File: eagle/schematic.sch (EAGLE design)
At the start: 32 parts, among them U1 PIC18F252-I/SP

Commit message: PCB in progress
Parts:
- added 5V, AN0, VBAT: TPPAD1-13, testpad:TPPAD1-13
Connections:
- net 5V: now also 5V.TP
- net AN0: now also AN0.TP
- net VBAT: now also VBAT.TP
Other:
- note added: "Title: PIC18F252 Binary Clock Author: Michel Lavoie Revision: 0.1.0 Date: 2016-11-26"
- note removed: "0.1.0"
- note removed: "1/1"
- note removed: "PIC18F252 Binary Clock"
- moved on the sheet: ADJ, BAT, C1, D1, D2, HR, MIN, PROG, R1, R10, R11, R12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

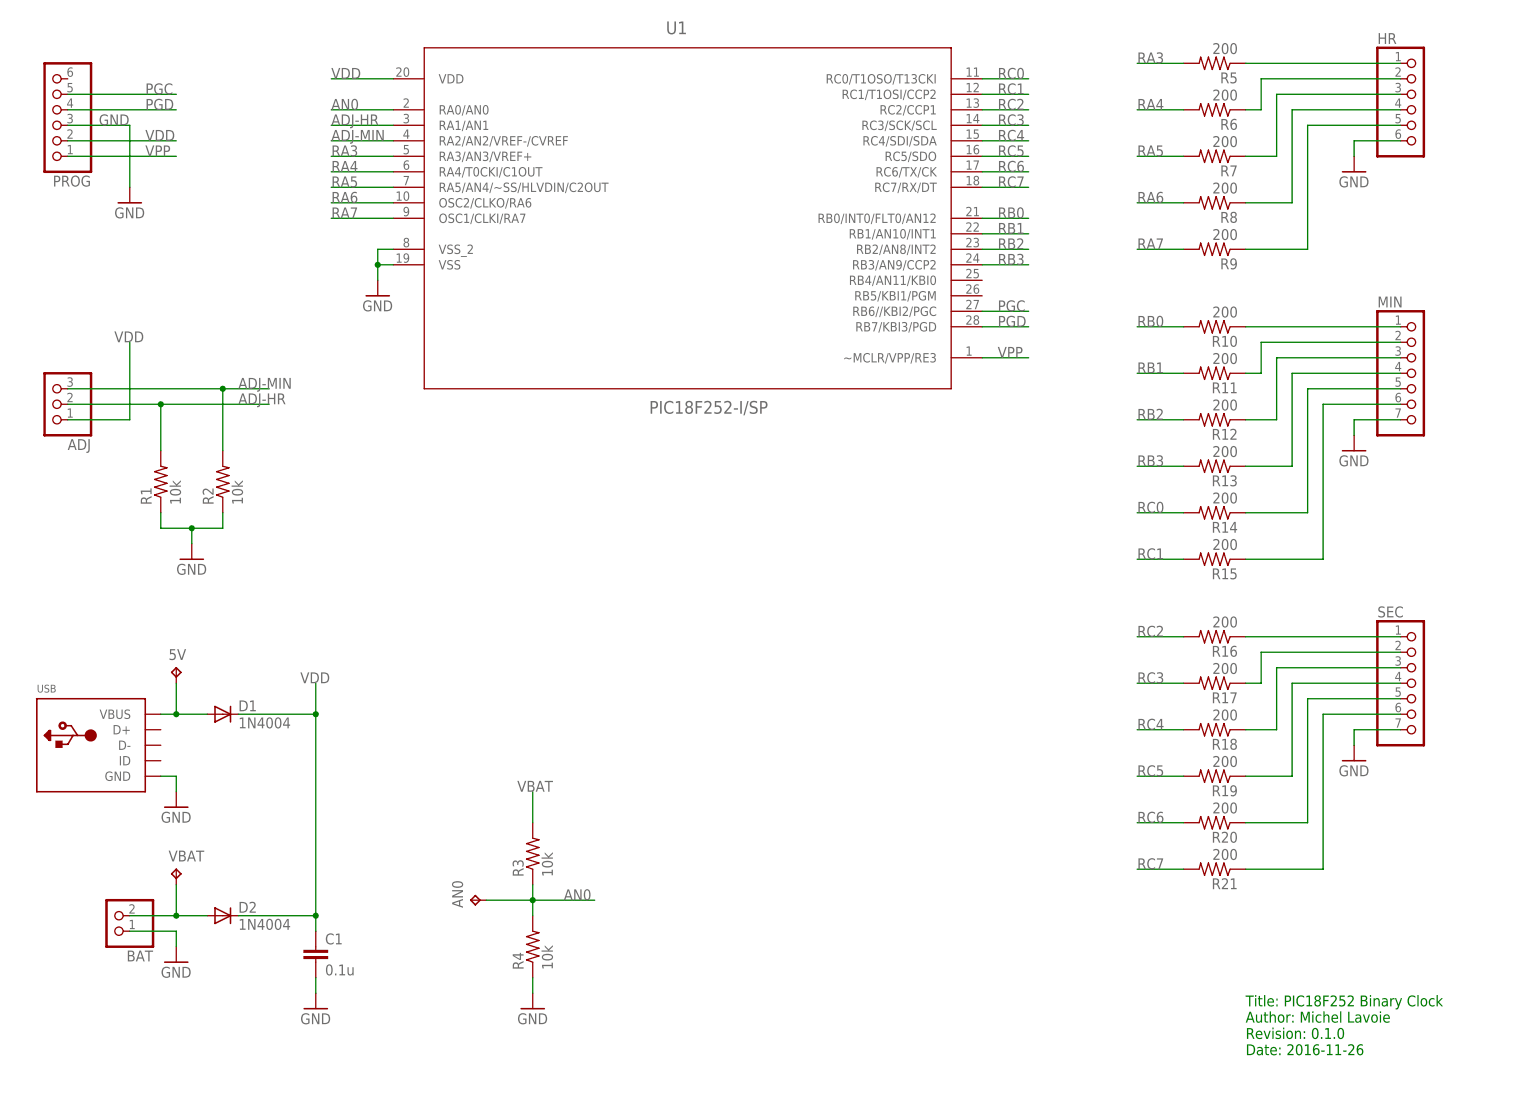
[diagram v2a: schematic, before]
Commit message: Version 0.1.1. Applied all items in the To Do list.
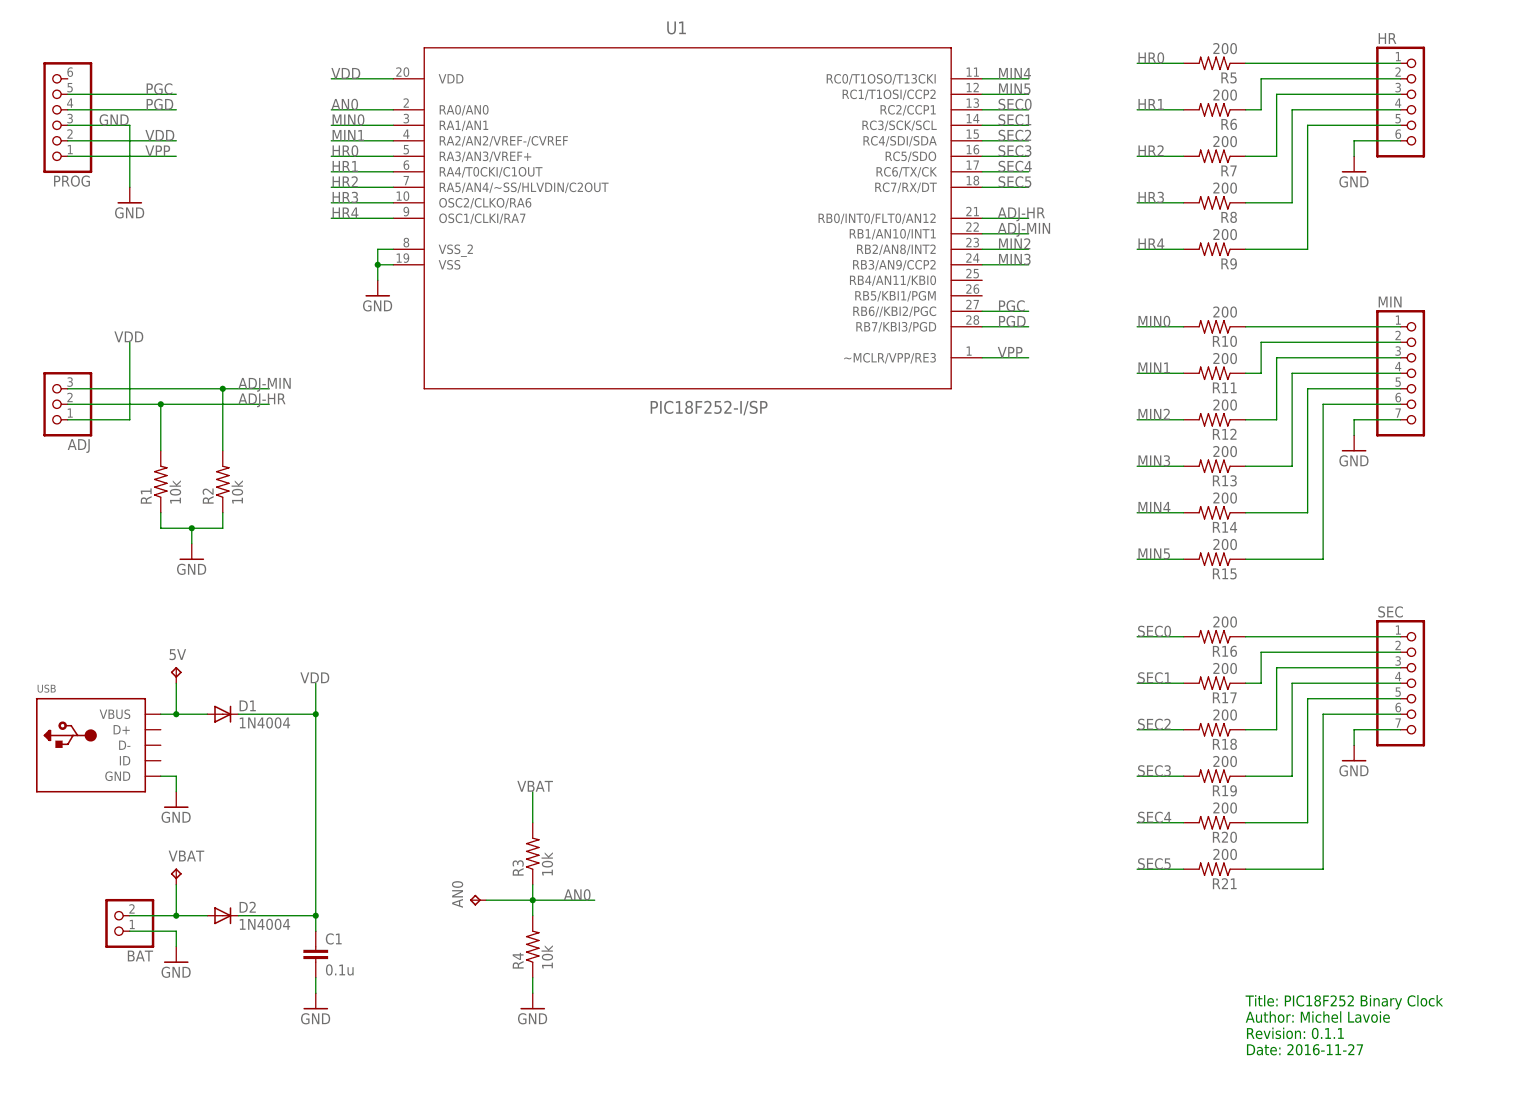
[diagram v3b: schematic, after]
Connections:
- net RA3 renamed HR0
- net RA4 renamed HR1
- net RA5 renamed HR2
- net RA6 renamed HR3
- net RA7 renamed HR4
- net RB2 renamed MIN2
- net RB3 renamed MIN3
- net RC0 renamed MIN4
- net RC1 renamed MIN5
- net RC2 renamed SEC0
- net RC3 renamed SEC1
- net RC4 renamed SEC2
- net RC5 renamed SEC3
- net RC6 renamed SEC4
- net RC7 renamed SEC5
- removed net RB0: R10.2, U1.RB0/INT0/FLT0/AN12
- removed net RB1: R11.2, U1.RB1/AN10/INT1
- new net MIN0: R10.2, U1.RA1/AN1
- new net MIN1: R11.2, U1.RA2/AN2/VREF-/CVREF
- net ADJ-HR: now also U1.RB0/INT0/FLT0/AN12; no longer U1.RA1/AN1
- net ADJ-MIN: now also U1.RB1/AN10/INT1; no longer U1.RA2/AN2/VREF-/CVREF
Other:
- note added: "Title: PIC18F252 Binary Clock Author: Michel Lavoie Revision: 0.1.1 Date: 2016-11-27"
- note removed: "Title: PIC18F252 Binary Clock Author: Michel Lavoie Revision: 0.1.0 Date: 2016-11-26"
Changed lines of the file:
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@@
 <text x="208.28" y="7.62" size="1.778" layer="91">Title: PIC18F252 Binary Clock
 Author: Michel Lavoie
-Revision: 0.1.0
-Date: 2016-11-26</text>
+Revision: 0.1.1
+Date: 2016-11-27</text>
 </plain>
 <instances>
@@
 </segment>
 <segment>
-<pinref part="U1" gate="A" pin="RA1/AN1"/>
-<wire x1="58.42" y1="160.02" x2="68.58" y2="160.02" width="0.1524" layer="91"/>
-<label x="58.42" y="160.02" size="1.778" layer="95"/>
+<pinref part="U1" gate="A" pin="RB0/INT0/FLT0/AN12"/>
+<wire x1="172.72" y1="144.78" x2="165.1" y2="144.78" width="0.1524" layer="91"/>
+<label x="167.64" y="144.78" size="1.778" layer="95"/>
 </segment>
 </net>
@@
 </segment>
 <segment>
-<pinref part="U1" gate="A" pin="RA2/AN2/VREF-/CVREF"/>
-<wire x1="58.42" y1="157.48" x2="68.58" y2="157.48" width="0.1524" layer="91"/>
-<label x="58.42" y="157.48" size="1.778" layer="95"/>
+<pinref part="U1" gate="A" pin="RB1/AN10/INT1"/>
+<wire x1="172.72" y1="142.24" x2="165.1" y2="142.24" width="0.1524" layer="91"/>
+<label x="167.64" y="142.24" size="1.778" layer="95"/>
 </segment>
 </net>
@@
 </segment>
 </net>
-<net name="RA3" class="0">
+<net name="HR0" class="0">
 <segment>
 <pinref part="U1" gate="A" pin="RA3/AN3/VREF+"/>
@@
 </segment>
 </net>
-<net name="RA4" class="0">
+<net name="HR1" class="0">
 <segment>
 <pinref part="U1" gate="A" pin="RA4/T0CKI/C1OUT"/>
@@
 </segment>
 </net>
-<net name="RA5" class="0">
+<net name="HR2" class="0">
 <segment>
 <pinref part="U1" gate="A" pin="RA5/AN4/~SS/HLVDIN/C2OUT"/>
@@
 </segment>
 </net>
-<net name="RA6" class="0">
+<net name="HR3" class="0">
 <segment>
 <pinref part="U1" gate="A" pin="OSC2/CLKO/RA6"/>
@@
 </segment>
 </net>
-<net name="RA7" class="0">
+<net name="HR4" class="0">
 <segment>
 <pinref part="U1" gate="A" pin="OSC1/CLKI/RA7"/>
@@
 </segment>
 </net>
-<net name="RC0" class="0">
+<net name="MIN4" class="0">
 <segment>
 <pinref part="U1" gate="A" pin="RC0/T1OSO/T13CKI"/>
@@
 </segment>
 </net>
-<net name="RC1" class="0">
+<net name="MIN5" class="0">
 <segment>
 <pinref part="U1" gate="A" pin="RC1/T1OSI/CCP2"/>
@@
 </segment>
 </net>
-<net name="RC2" class="0">
+<net name="SEC0" class="0">
 <segment>
 <pinref part="U1" gate="A" pin="RC2/CCP1"/>
@@
 </segment>
 </net>
-<net name="RC3" class="0">
+<net name="SEC1" class="0">
 <segment>
 <pinref part="U1" gate="A" pin="RC3/SCK/SCL"/>
@@
 </segment>
 </net>
-<net name="RC4" class="0">
+<net name="SEC2" class="0">
 <segment>
 <pinref part="U1" gate="A" pin="RC4/SDI/SDA"/>
@@
 </segment>
 </net>
-<net name="RC5" class="0">
+<net name="SEC3" class="0">
 <segment>
 <pinref part="U1" gate="A" pin="RC5/SDO"/>
@@
 </segment>
 </net>
-<net name="RC6" class="0">
+<net name="SEC4" class="0">
 <segment>
 <pinref part="U1" gate="A" pin="RC6/TX/CK"/>
@@
 </segment>
 </net>
-<net name="RC7" class="0">
+<net name="SEC5" class="0">
 <segment>
 <pinref part="U1" gate="A" pin="RC7/RX/DT"/>
@@
 </segment>
 </net>
-<net name="RB0" class="0">
-<segment>
-<pinref part="U1" gate="A" pin="RB0/INT0/FLT0/AN12"/>
-<wire x1="172.72" y1="144.78" x2="165.1" y2="144.78" width="0.1524" layer="91"/>
-<label x="167.64" y="144.78" size="1.778" layer="95"/>
+<net name="MIN2" class="0">
+<segment>
+<pinref part="U1" gate="A" pin="RB2/AN8/INT2"/>
+<wire x1="172.72" y1="139.7" x2="165.1" y2="139.7" width="0.1524" layer="91"/>
+<label x="167.64" y="139.7" size="1.778" layer="95"/>
+</segment>
+<segment>
+<pinref part="R12" gate="G$1" pin="2"/>
+<wire x1="190.5" y1="111.76" x2="198.12" y2="111.76" width="0.1524" layer="91"/>
+<label x="190.5" y="111.76" size="1.778" layer="95"/>
+</segment>
+</net>
+<net name="MIN3" class="0">
+<segment>
+<pinref part="U1" gate="A" pin="RB3/AN9/CCP2"/>
+<wire x1="172.72" y1="137.16" x2="165.1" y2="137.16" width="0.1524" layer="91"/>
+<label x="167.64" y="137.16" size="1.778" layer="95"/>
+</segment>
+<segment>
+<pinref part="R13" gate="G$1" pin="2"/>
+<wire x1="190.5" y1="104.14" x2="198.12" y2="104.14" width="0.1524" layer="91"/>
+<label x="190.5" y="104.14" size="1.778" layer="95"/>
+</segment>
+</net>
+<net name="MIN0" class="0">
+<segment>
+<pinref part="U1" gate="A" pin="RA1/AN1"/>
+<wire x1="58.42" y1="160.02" x2="68.58" y2="160.02" width="0.1524" layer="91"/>
+<label x="58.42" y="160.02" size="1.778" layer="95"/>
 </segment>
 <segment>
@@
 </segment>
 </net>
-<net name="RB1" class="0">
-<segment>
-<pinref part="U1" gate="A" pin="RB1/AN10/INT1"/>
-<wire x1="172.72" y1="142.24" x2="165.1" y2="142.24" width="0.1524" layer="91"/>
-<label x="167.64" y="142.24" size="1.778" layer="95"/>
+<net name="MIN1" class="0">
+<segment>
+<pinref part="U1" gate="A" pin="RA2/AN2/VREF-/CVREF"/>
+<wire x1="58.42" y1="157.48" x2="68.58" y2="157.48" width="0.1524" layer="91"/>
+<label x="58.42" y="157.48" size="1.778" layer="95"/>
 </segment>
 <segment>
@@
 </segment>
 </net>
-<net name="RB2" class="0">
-<segment>
-<pinref part="U1" gate="A" pin="RB2/AN8/INT2"/>
-<wire x1="172.72" y1="139.7" x2="165.1" y2="139.7" width="0.1524" layer="91"/>
-<label x="167.64" y="139.7" size="1.778" layer="95"/>
-</segment>
-<segment>
-<pinref part="R12" gate="G$1" pin="2"/>
-<wire x1="190.5" y1="111.76" x2="198.12" y2="111.76" width="0.1524" layer="91"/>
-<label x="190.5" y="111.76" size="1.778" layer="95"/>
-</segment>
-</net>
-<net name="RB3" class="0">
-<segment>
-<pinref part="U1" gate="A" pin="RB3/AN9/CCP2"/>
-<wire x1="172.72" y1="137.16" x2="165.1" y2="137.16" width="0.1524" layer="91"/>
-<label x="167.64" y="137.16" size="1.778" layer="95"/>
-</segment>
-<segment>
-<pinref part="R13" gate="G$1" pin="2"/>
-<wire x1="190.5" y1="104.14" x2="198.12" y2="104.14" width="0.1524" layer="91"/>
-<label x="190.5" y="104.14" size="1.778" layer="95"/>
-</segment>
-</net>

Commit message: Corrigé les bugs restants, mis à jour la documentation
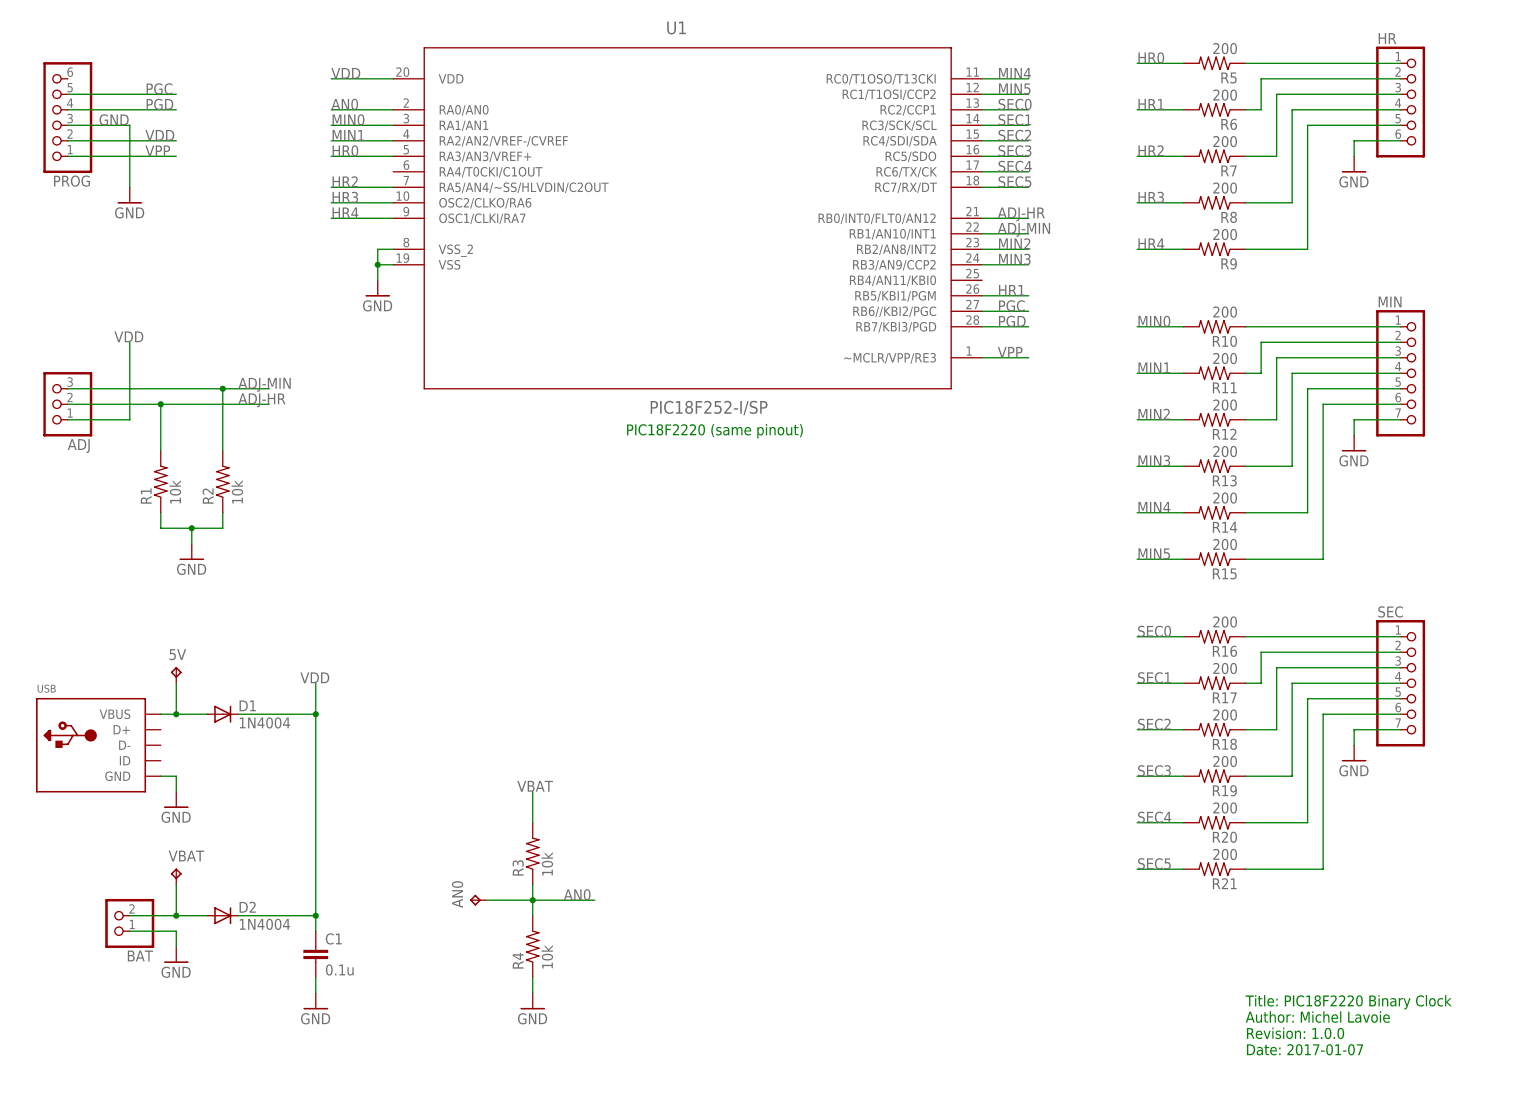
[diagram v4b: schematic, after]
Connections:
- net HR1: now also U1.RB5/KBI1/PGM; no longer U1.RA4/T0CKI/C1OUT
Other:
- note added: "PIC18F2220 (same pinout)"
- note added: "Title: PIC18F2220 Binary Clock Author: Michel Lavoie Revision: 1.0.0 Date: 2017-01-07"
- note removed: "Title: PIC18F252 Binary Clock Author: Michel Lavoie Revision: 0.1.1 Date: 2016-11-27"
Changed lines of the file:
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@@
 <sheet>
 <plain>
-<text x="208.28" y="7.62" size="1.778" layer="91">Title: PIC18F252 Binary Clock
+<text x="208.28" y="7.62" size="1.778" layer="91">Title: PIC18F2220 Binary Clock
 Author: Michel Lavoie
-Revision: 0.1.1
-Date: 2016-11-27</text>
+Revision: 1.0.0
+Date: 2017-01-07</text>
+<text x="106.68" y="109.22" size="1.778" layer="91">PIC18F2220 (same pinout)</text>
 </plain>
 <instances>
@@
 <net name="HR1" class="0">
 <segment>
-<pinref part="U1" gate="A" pin="RA4/T0CKI/C1OUT"/>
-<wire x1="58.42" y1="152.4" x2="68.58" y2="152.4" width="0.1524" layer="91"/>
-<label x="58.42" y="152.4" size="1.778" layer="95"/>
-</segment>
-<segment>
 <pinref part="R6" gate="G$1" pin="2"/>
 <wire x1="190.5" y1="162.56" x2="198.12" y2="162.56" width="0.1524" layer="91"/>
 <label x="190.5" y="162.56" size="1.778" layer="95"/>
 </segment>
-</net>
+<segment>
+<pinref part="U1" gate="A" pin="RB5/KBI1/PGM"/>
+<wire x1="172.72" y1="132.08" x2="165.1" y2="132.08" width="0.1524" layer="91"/>
+<label x="167.64" y="132.08" size="1.778" layer="95"/>
+</segment>
+</net>
